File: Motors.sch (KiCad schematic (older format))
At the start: 5 parts

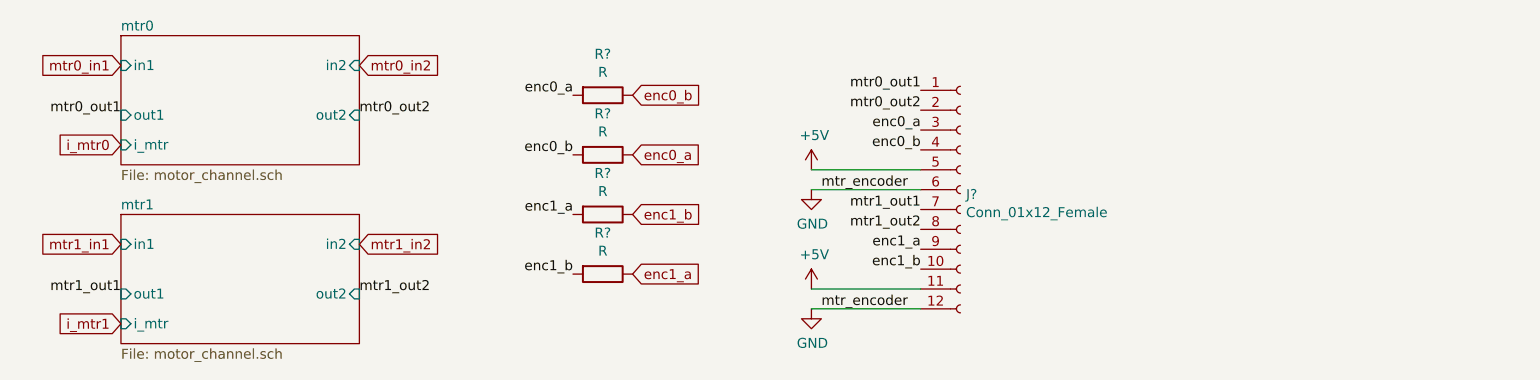
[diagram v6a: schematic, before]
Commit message: added dual inpt and gate control
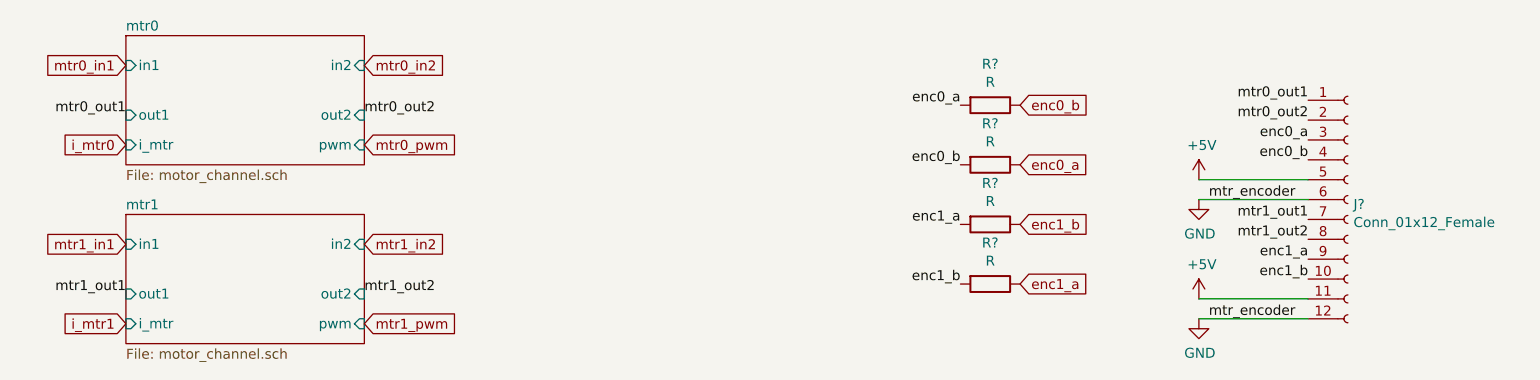
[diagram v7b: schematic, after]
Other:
- moved on the sheet: J?, R?
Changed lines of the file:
@@
 $EndDescr
 $Sheet
-S 3525 1350 1200 650
+S 3550 1350 1200 650
 U 5E507A5C
 F0 "mtr0" 50
 F1 "motor_channel.sch" 50
-F2 "in1" I L 3525 1500 50
-F3 "in2" I R 4725 1500 50
-F4 "i_mtr" I L 3525 1900 50
-F5 "out1" I L 3525 1750 50
-F6 "out2" I R 4725 1750 50
+F2 "in1" I L 3550 1500 50
+F3 "in2" I R 4750 1500 50
+F4 "i_mtr" I L 3550 1900 50
+F5 "out1" I L 3550 1750 50
+F6 "out2" I R 4750 1750 50
+F7 "pwm" I R 4750 1900 50
 $EndSheet
-Text Label 3525 1750 2    50   ~ 0
+Text Label 3550 1750 2    50   ~ 0
 mtr0_out1
-Text Label 4725 1750 0    50   ~ 0
+Text Label 4750 1750 0    50   ~ 0
 mtr0_out2
-Text GLabel 3525 1500 0    50   Input ~ 0
+Text GLabel 3550 1500 0    50   Input ~ 0
 mtr0_in1
-Text GLabel 4725 1500 2    50   Input ~ 0
+Text GLabel 4750 1500 2    50   Input ~ 0
 mtr0_in2
-Text GLabel 3525 1900 0    50   Input ~ 0
+Text GLabel 3550 1900 0    50   Input ~ 0
 i_mtr0
 $Comp
 L Connector:Conn_01x12_Female J?
 U 1 1 5E6AD3E3
-P 7750 2125
-F 0 "J?" H 7778 2101 50  0000 L CNN
-F 1 "Conn_01x12_Female" H 7778 2010 50  0000 L CNN
-F 2 "" H 7750 2125 50  0001 C CNN
-F 3 "~" H 7750 2125 50  0001 C CNN
-	1    7750 2125
+P 9700 2175
+F 0 "J?" H 9728 2151 50  0000 L CNN
+F 1 "Conn_01x12_Female" H 9728 2060 50  0000 L CNN
+F 2 "" H 9700 2175 50  0001 C CNN
+F 3 "~" H 9700 2175 50  0001 C CNN
+	1    9700 2175
 	1    0    0    -1
 $EndComp
-Text Label 7550 1625 2    50   ~ 0
+Text Label 9500 1675 2    50   ~ 0
 mtr0_out1
-Text Label 7550 1725 2    50   ~ 0
+Text Label 9500 1775 2    50   ~ 0
 mtr0_out2
-Text GLabel 6100 1950 2    50   Input ~ 0
+Text GLabel 8050 2000 2    50   Input ~ 0
 enc0_a
-Text Label 7550 2225 2    50   ~ 0
+Text Label 9500 2275 2    50   ~ 0
 mtr1_out1
-Text Label 7550 2325 2    50   ~ 0
+Text Label 9500 2375 2    50   ~ 0
 mtr1_out2
-Text GLabel 6100 2550 2    50   Input ~ 0
+Text GLabel 8050 2600 2    50   Input ~ 0
 enc1_a
-Text GLabel 6100 2250 2    50   Input ~ 0
+Text GLabel 8050 2300 2    50   Input ~ 0
 enc1_b
 Wire Wire Line
-	7000 2025 7550 2025
+	8950 2075 9500 2075
 Wire Wire Line
-	7000 2125 7550 2125
+	8950 2175 9500 2175
 Wire Wire Line
-	7000 2625 7550 2625
+	8950 2675 9500 2675
 Wire Wire Line
-	7000 2725 7550 2725
+	8950 2775 9500 2775
 $Comp
 L power:+5V #PWR?
 U 1 1 5E6B0E85
-P 7000 2025
-F 0 "#PWR?" H 7000 1875 50  0001 C CNN
-F 1 "+5V" H 7015 2198 50  0000 C CNN
-F 2 "" H 7000 2025 50  0001 C CNN
-F 3 "" H 7000 2025 50  0001 C CNN
-	1    7000 2025
+P 8950 2075
+F 0 "#PWR?" H 8950 1925 50  0001 C CNN
+F 1 "+5V" H 8965 2248 50  0000 C CNN
+F 2 "" H 8950 2075 50  0001 C CNN
+F 3 "" H 8950 2075 50  0001 C CNN
+	1    8950 2075
 	1    0    0    -1
 $EndComp
@@
 L power:+5V #PWR?
 U 1 1 5E6B1311
-P 7000 2625
-F 0 "#PWR?" H 7000 2475 50  0001 C CNN
-F 1 "+5V" H 7015 2798 50  0000 C CNN
-F 2 "" H 7000 2625 50  0001 C CNN
-F 3 "" H 7000 2625 50  0001 C CNN
-	1    7000 2625
+P 8950 2675
+F 0 "#PWR?" H 8950 2525 50  0001 C CNN
+F 1 "+5V" H 8965 2848 50  0000 C CNN
+F 2 "" H 8950 2675 50  0001 C CNN
+F 3 "" H 8950 2675 50  0001 C CNN
+	1    8950 2675
 	1    0    0    -1
 $EndComp
@@
 L power:GND #PWR?
 U 1 1 5E6B1444
-P 7000 2125
-F 0 "#PWR?" H 7000 1875 50  0001 C CNN
-F 1 "GND" H 7005 1952 50  0000 C CNN
-F 2 "" H 7000 2125 50  0001 C CNN
-F 3 "" H 7000 2125 50  0001 C CNN
-	1    7000 2125
+P 8950 2175
+F 0 "#PWR?" H 8950 1925 50  0001 C CNN
+F 1 "GND" H 8955 2002 50  0000 C CNN
+F 2 "" H 8950 2175 50  0001 C CNN
+F 3 "" H 8950 2175 50  0001 C CNN
+	1    8950 2175
 	1    0    0    -1
 $EndComp
@@
 L power:GND #PWR?
 U 1 1 5E6B180E
-P 7000 2725
-F 0 "#PWR?" H 7000 2475 50  0001 C CNN
-F 1 "GND" H 7005 2552 50  0000 C CNN
-F 2 "" H 7000 2725 50  0001 C CNN
-F 3 "" H 7000 2725 50  0001 C CNN
-	1    7000 2725
+P 8950 2775
+F 0 "#PWR?" H 8950 2525 50  0001 C CNN
+F 1 "GND" H 8955 2602 50  0000 C CNN
+F 2 "" H 8950 2775 50  0001 C CNN
+F 3 "" H 8950 2775 50  0001 C CNN
+	1    8950 2775
 	1    0    0    -1
 $EndComp
-Text Label 7050 2725 0    50   ~ 0
+Text Label 9000 2775 0    50   ~ 0
 mtr_encoder
-Text Label 7050 2125 0    50   ~ 0
+Text Label 9000 2175 0    50   ~ 0
 mtr_encoder
-Text GLabel 6100 1650 2    50   Input ~ 0
+Text GLabel 8050 1700 2    50   Input ~ 0
 enc0_b
 $Sheet
-S 3525 2250 1200 650
+S 3550 2250 1200 650
 U 5E6EF1BC
 F0 "mtr1" 50
 F1 "motor_channel.sch" 50
-F2 "in1" I L 3525 2400 50
-F3 "in2" I R 4725 2400 50
-F4 "i_mtr" I L 3525 2800 50
-F5 "out1" I L 3525 2650 50
-F6 "out2" I R 4725 2650 50
+F2 "in1" I L 3550 2400 50
+F3 "in2" I R 4750 2400 50
+F4 "i_mtr" I L 3550 2800 50
+F5 "out1" I L 3550 2650 50
+F6 "out2" I R 4750 2650 50
+F7 "pwm" I R 4750 2800 50
 $EndSheet
-Text Label 3525 2650 2    50   ~ 0
+Text Label 3550 2650 2    50   ~ 0
 mtr1_out1
-Text Label 4725 2650 0    50   ~ 0
+Text Label 4750 2650 0    50   ~ 0
 mtr1_out2
-Text GLabel 3525 2400 0    50   Input ~ 0
+Text GLabel 3550 2400 0    50   Input ~ 0
 mtr1_in1
-Text GLabel 4725 2400 2    50   Input ~ 0
+Text GLabel 4750 2400 2    50   Input ~ 0
 mtr1_in2
-Text GLabel 3525 2800 0    50   Input ~ 0
+Text GLabel 3550 2800 0    50   Input ~ 0
 i_mtr1
 $Comp
 L Device:R R?
 U 1 1 5E6FBB13
-P 5950 1650
-F 0 "R?" V 5743 1650 50  0000 C CNN
-F 1 "R" V 5834 1650 50  0000 C CNN
-F 2 "" V 5880 1650 50  0001 C CNN
-F 3 "~" H 5950 1650 50  0001 C CNN
-	1    5950 1650
+P 7900 1700
+F 0 "R?" V 7693 1700 50  0000 C CNN
+F 1 "R" V 7784 1700 50  0000 C CNN
+F 2 "" V 7830 1700 50  0001 C CNN
+F 3 "~" H 7900 1700 50  0001 C CNN
+	1    7900 1700
 	0    1    1    0
 $EndComp
-Text Label 7550 1825 2    50   ~ 0
+Text Label 9500 1875 2    50   ~ 0
 enc0_a
-Text Label 7550 1925 2    50   ~ 0
+Text Label 9500 1975 2    50   ~ 0
 enc0_b
-Text Label 7550 2425 2    50   ~ 0
+Text Label 9500 2475 2    50   ~ 0
 enc1_a
-Text Label 7550 2525 2    50   ~ 0
+Text Label 9500 2575 2    50   ~ 0
 enc1_b
-Text Label 5800 1650 2    50   ~ 0
+Text Label 7750 1700 2    50   ~ 0
 enc0_a
-Text Label 5800 1950 2    50   ~ 0
+Text Label 7750 2000 2    50   ~ 0
 enc0_b
 $Comp
 L Device:R R?
 U 1 1 5E700368
-P 5950 1950
-F 0 "R?" V 5743 1950 50  0000 C CNN
-F 1 "R" V 5834 1950 50  0000 C CNN
-F 2 "" V 5880 1950 50  0001 C CNN
-F 3 "~" H 5950 1950 50  0001 C CNN
-	1    5950 1950
+P 7900 2000
+F 0 "R?" V 7693 2000 50  0000 C CNN
+F 1 "R" V 7784 2000 50  0000 C CNN
+F 2 "" V 7830 2000 50  0001 C CNN
+F 3 "~" H 7900 2000 50  0001 C CNN
+	1    7900 2000
 	0    1    1    0
 $EndComp
@@
 L Device:R R?
 U 1 1 5E701D8F
-P 5950 2250
-F 0 "R?" V 5743 2250 50  0000 C CNN
-F 1 "R" V 5834 2250 50  0000 C CNN
-F 2 "" V 5880 2250 50  0001 C CNN
-F 3 "~" H 5950 2250 50  0001 C CNN
-	1    5950 2250
+P 7900 2300
+F 0 "R?" V 7693 2300 50  0000 C CNN
+F 1 "R" V 7784 2300 50  0000 C CNN
+F 2 "" V 7830 2300 50  0001 C CNN
+F 3 "~" H 7900 2300 50  0001 C CNN
+	1    7900 2300
 	0    1    1    0
 $EndComp
@@
 L Device:R R?
 U 1 1 5E7027C7
-P 5950 2550
-F 0 "R?" V 5743 2550 50  0000 C CNN
-F 1 "R" V 5834 2550 50  0000 C CNN
-F 2 "" V 5880 2550 50  0001 C CNN
-F 3 "~" H 5950 2550 50  0001 C CNN
-	1    5950 2550
+P 7900 2600
+F 0 "R?" V 7693 2600 50  0000 C CNN
+F 1 "R" V 7784 2600 50  0000 C CNN
+F 2 "" V 7830 2600 50  0001 C CNN
+F 3 "~" H 7900 2600 50  0001 C CNN
+	1    7900 2600
 	0    1    1    0
 $EndComp
-Text Label 5800 2250 2    50   ~ 0
+Text Label 7750 2300 2    50   ~ 0
 enc1_a
-Text Label 5800 2550 2    50   ~ 0
+Text Label 7750 2600 2    50   ~ 0
 enc1_b
+Text GLabel 4750 1900 2    50   Input ~ 0
+mtr0_pwm
+Text GLabel 4750 2800 2    50   Input ~ 0
+mtr1_pwm
 $EndSCHEMATC

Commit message: Motor capacitors, test points, jumpers
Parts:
- added JP? (x6): Jumper, symbol Device:Jumper
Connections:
- net +5V: now also JP?.1, JP?.1; no longer J?.11 (Pin_11), J?.5 (Pin_5)
- new net +12V: JP?.1, JP?.1
- new net +3V3: JP?.1, JP?.1
- new net p_enc0: J?.5 (Pin_5), JP?.2, JP?.2, JP?.2
- new net p_enc1: J?.11 (Pin_11), JP?.2, JP?.2, JP?.2
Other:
- moved on the sheet: J?, R?
